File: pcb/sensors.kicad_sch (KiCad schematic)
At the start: 0 parts

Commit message: add sensors, hierarchical changes
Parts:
- added U?: MCP9804_DFN, Package_DFN_QFN:DFN-8-1EP_3x2mm_P0.5mm_EP1.7x1.4mm, symbol Sensor_Temperature:MCP9804_DFN
- added U?: INA230AIRGTT, Package_DFN_QFN:VQFN-16-1EP_3x3mm_P0.5mm_EP1.6x1.6mm, symbol Sensor_Current:INA230AIRGTT
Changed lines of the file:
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@@
 	(generator_version "9.0")
 	(paper "A4")
+	(symbol
+		(lib_id "Sensor_Temperature:MCP9804_DFN")
+		(at 130.81 54.61 0)
+		(unit 1)
+		(exclude_from_sim no)
+		(in_bom yes)
+		(on_board yes)
+		(dnp no)
+		(fields_autoplaced yes)
+		(property "Reference" "U?"
+			(at 146.05 48.1898 0)
+			(effects
+				(font
+					(size 1.27 1.27)
+				)
+			)
+		)
+		(property "Value" "MCP9804_DFN"
+			(at 146.05 50.7298 0)
+			(effects
+				(font
+					(size 1.27 1.27)
+				)
+			)
+		)
+		(property "Footprint" "Package_DFN_QFN:DFN-8-1EP_3x2mm_P0.5mm_EP1.7x1.4mm"
+			(at 130.81 54.61 0)
+			(effects
+				(font
+					(size 1.27 1.27)
+				)
+				(hide yes)
+			)
+		)
+		(property "Datasheet" "http://ww1.microchip.com/downloads/en/DeviceDoc/22203b.pdf"
+			(at 124.46 43.18 0)
+			(effects
+				(font
+					(size 1.27 1.27)
+				)
+				(hide yes)
+			)
+		)
+		(property "Description" "±0.25°C (±1°C) Typical (Maximum), Digital Temperature Sensor, DFN-8"
+			(at 130.81 54.61 0)
+			(effects
+				(font
+					(size 1.27 1.27)
+				)
+				(hide yes)
+			)
+		)
+		(pin "8"
+		)
+		(pin "3"
+		)
+		(pin "2"
+		)
+		(pin "1"
+		)
+		(pin "5"
+		)
+		(pin "7"
+		)
+		(pin "6"
+		)
+		(pin "4"
+		)
+		(pin "9"
+		)
+		(instances
+			(project ""
+				(path "/e63e39d7-6ac0-4ffd-8aa3-1841a4541b55/010325a2-ae86-4ae0-96e8-1d16e8e45471"
+					(reference "U?")
+					(unit 1)
+				)
+			)
+		)
+	)
+	(symbol
+		(lib_id "Sensor_Current:INA230AIRGTT")
+		(at 73.66 55.88 0)
+		(unit 1)
+		(exclude_from_sim no)
+		(in_bom yes)
+		(on_board yes)
+		(dnp no)
+		(fields_autoplaced yes)
+		(property "Reference" "U?"
+			(at 73.66 36.83 0)
+			(effects
+				(font
+					(size 1.27 1.27)
+				)
+			)
+		)
+		(property "Value" "INA230AIRGTT"
+			(at 73.66 39.37 0)
+			(effects
+				(font
+					(size 1.27 1.27)
+				)
+			)
+		)
+		(property "Footprint" "Package_DFN_QFN:VQFN-16-1EP_3x3mm_P0.5mm_EP1.6x1.6mm"
+			(at 73.66 55.88 0)
+			(effects
+				(font
+					(size 1.27 1.27)
+				)
+				(hide yes)
+			)
+		)
+		(property "Datasheet" "https://www.ti.com/lit/ds/symlink/ina230.pdf?ts=1755978668271"
+			(at 73.66 55.88 0)
+			(effects
+				(font
+					(size 1.27 1.27)
+				)
+				(hide yes)
+			)
+		)
+		(property "Description" "36-V, 16-bit, I²C output current, voltage and power monitor with alert"
+			(at 73.66 55.88 0)
+			(effects
+				(font
+					(size 1.27 1.27)
+				)
+				(hide yes)
+			)
+		)
+		(pin "15"
+		)
+		(pin "17"
+		)
+		(pin "10"
+		)
+		(pin "4"
+		)
+		(pin "5"
+		)
+		(pin "16"
+		)
+		(pin "1"
+		)
+		(pin "12"
+		)
+		(pin "3"
+		)
+		(pin "11"
+		)
+		(pin "13"
+		)
+		(pin "2"
+		)
+		(pin "6"
+		)
+		(pin "7"
+		)
+		(pin "8"
+		)
+		(pin "8"
+		)
+		(pin "14"
+		)
+		(instances
+			(project ""
+				(path "/e63e39d7-6ac0-4ffd-8aa3-1841a4541b55/010325a2-ae86-4ae0-96e8-1d16e8e45471"
+					(reference "U?")
+					(unit 1)
+				)
+			)
+		)
+	)
 )

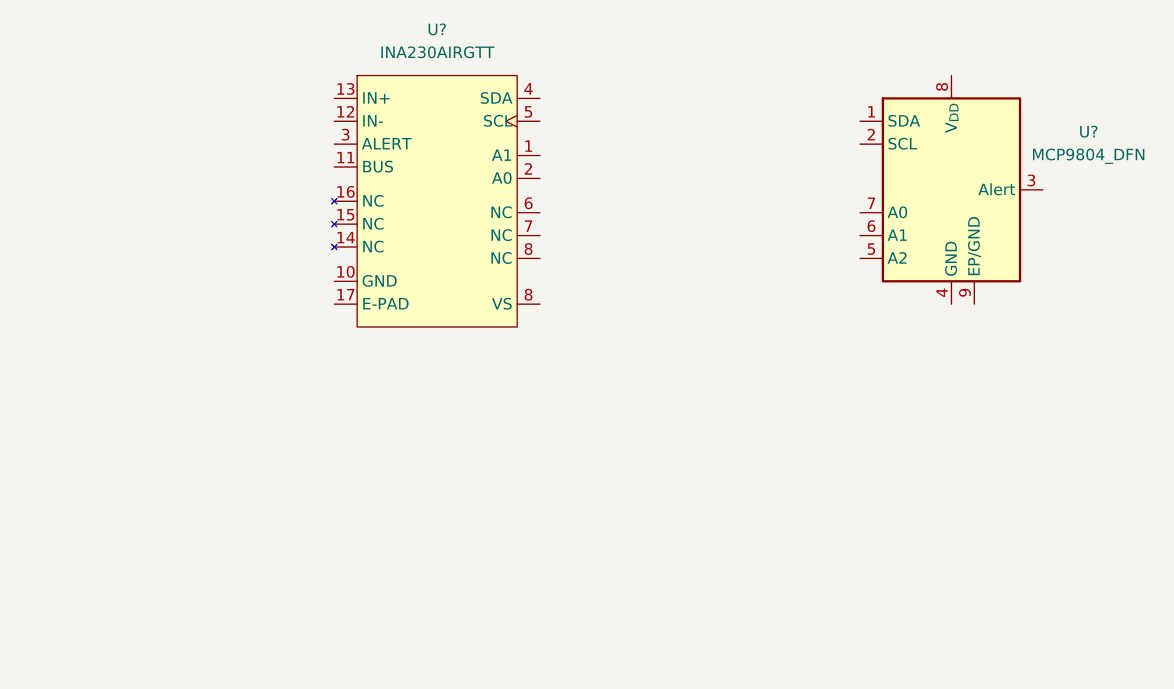
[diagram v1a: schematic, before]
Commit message: addl. updates to power hierarchy
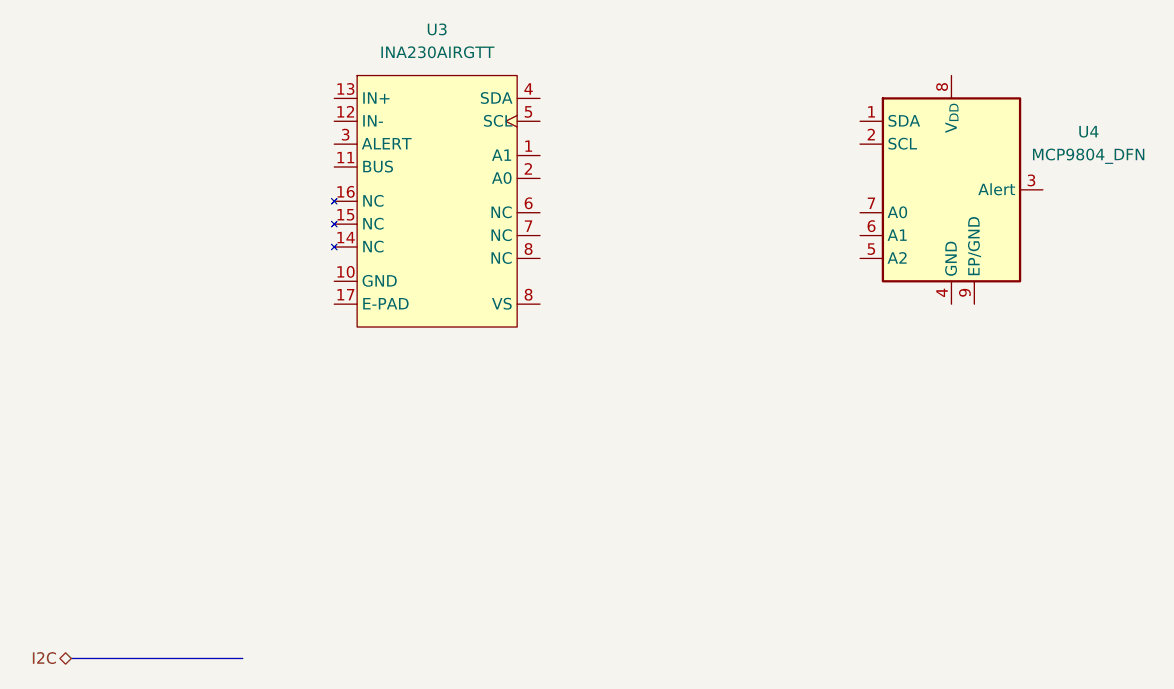
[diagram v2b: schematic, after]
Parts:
- gave numbers to parts that had none: 2
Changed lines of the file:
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@@
 	(generator_version "9.0")
 	(paper "A4")
+	(bus
+		(pts
+			(xy 33.02 106.68) (xy 52.07 106.68)
+		)
+		(stroke
+			(width 0)
+			(type default)
+		)
+	)
+	(hierarchical_label "I2C"
+		(shape bidirectional)
+		(at 33.02 106.68 180)
+		(effects
+			(font
+				(size 1.27 1.27)
+			)
+			(justify right)
+		)
+	)
 	(symbol
 		(lib_id "Sensor_Temperature:MCP9804_DFN")
@@
 		(dnp no)
 		(fields_autoplaced yes)
-		(property "Reference" "U?"
+		(property "Reference" "U4"
 			(at 146.05 48.1898 0)
 			(effects
@@
 			(project ""
 				(path "/e63e39d7-6ac0-4ffd-8aa3-1841a4541b55/010325a2-ae86-4ae0-96e8-1d16e8e45471"
-					(reference "U?")
+					(reference "U4")
 					(unit 1)
 				)
@@
 		(dnp no)
 		(fields_autoplaced yes)
-		(property "Reference" "U?"
+		(property "Reference" "U3"
 			(at 73.66 36.83 0)
 			(effects
@@
 			(project ""
 				(path "/e63e39d7-6ac0-4ffd-8aa3-1841a4541b55/010325a2-ae86-4ae0-96e8-1d16e8e45471"
-					(reference "U?")
+					(reference "U3")
 					(unit 1)
 				)

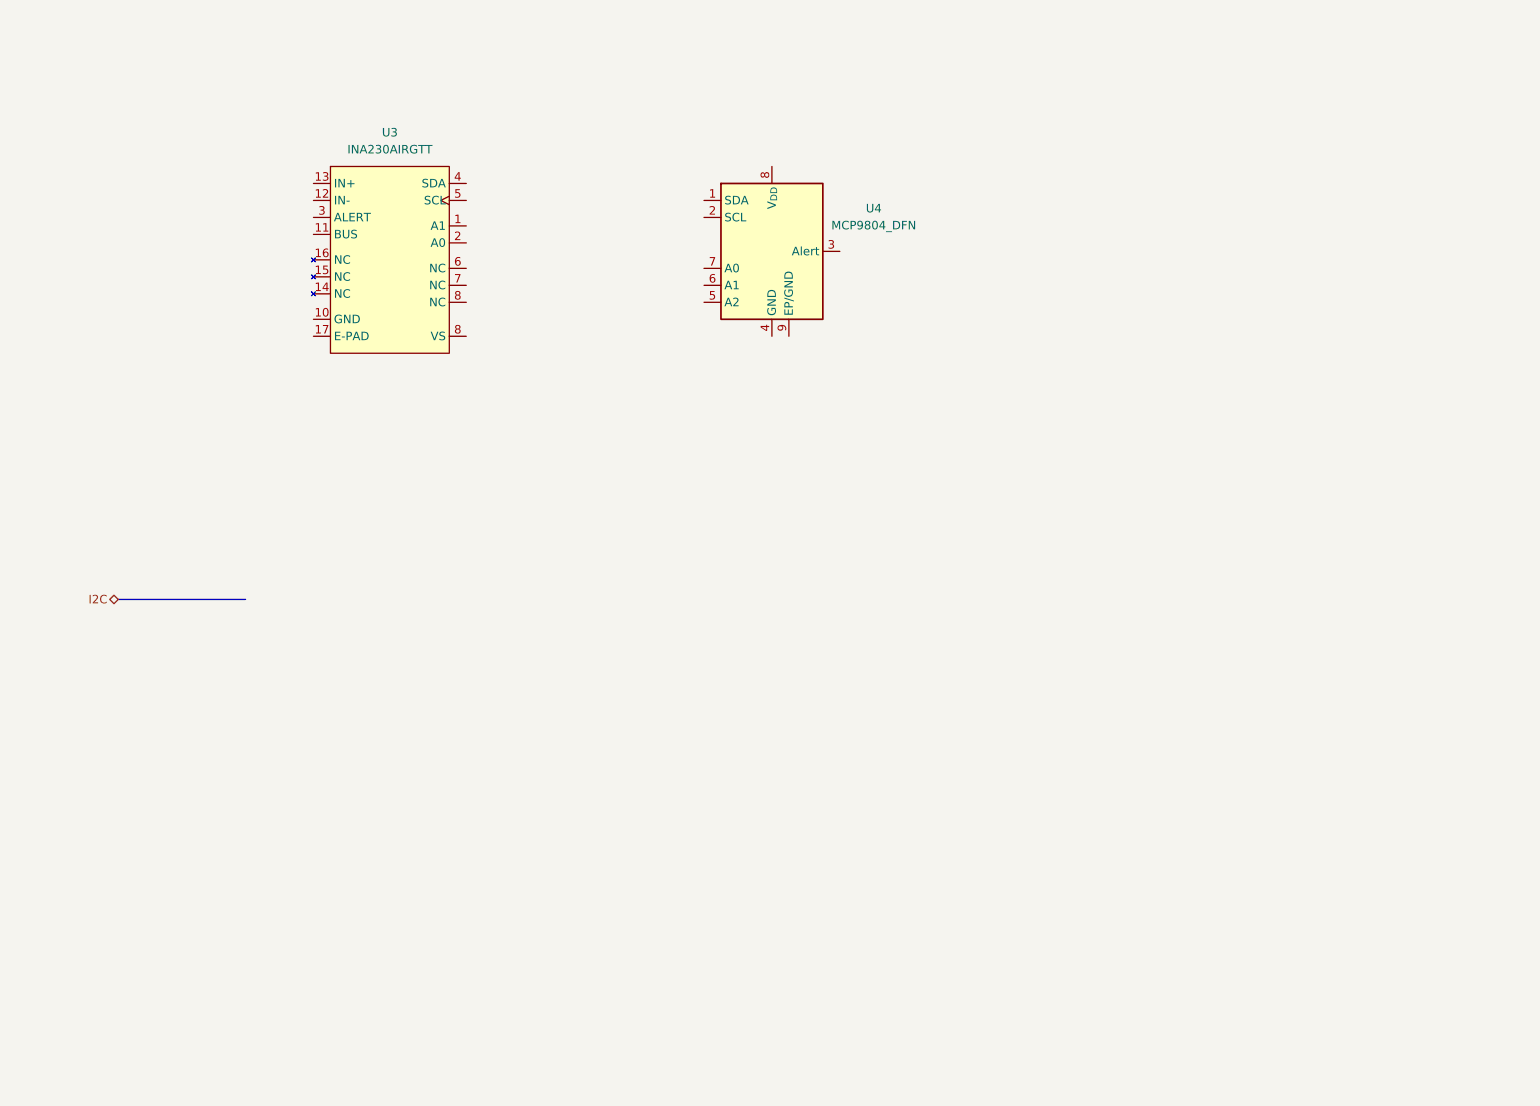
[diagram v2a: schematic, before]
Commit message: added power sequencing through raspi gpio
additionally defined sensors
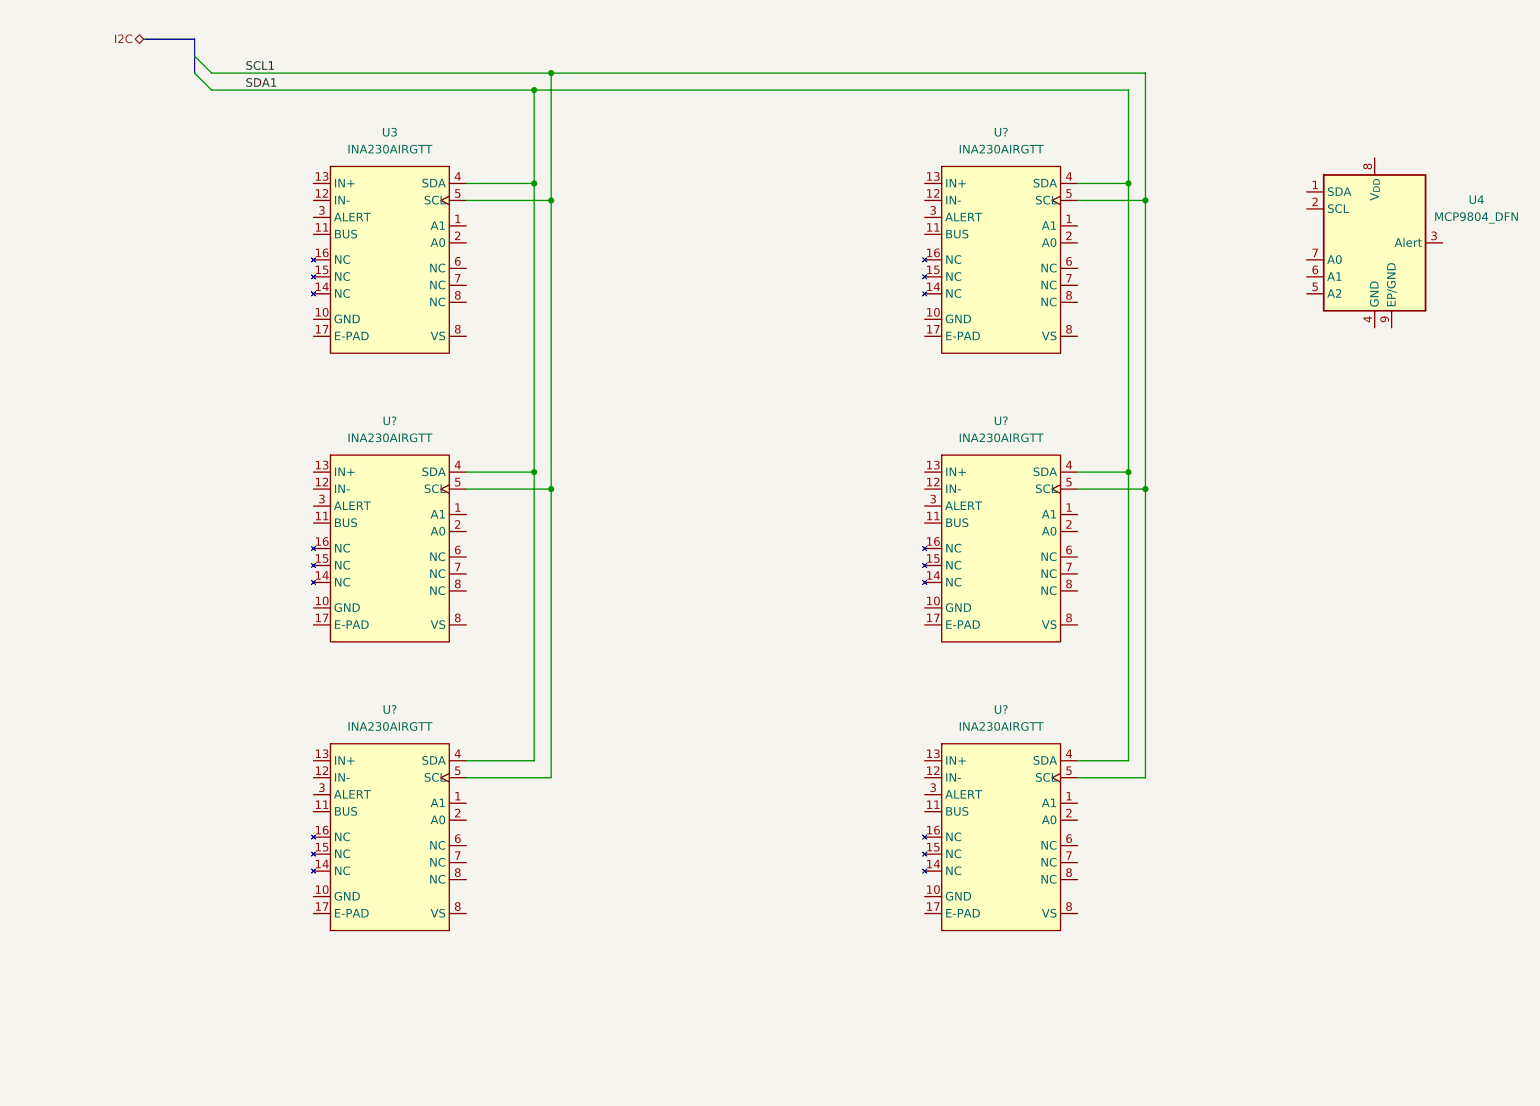
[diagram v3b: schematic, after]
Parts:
- added U? (x5): INA230AIRGTT, Package_DFN_QFN:VQFN-16-1EP_3x3mm_P0.5mm_EP1.6x1.6mm, symbol Sensor_Current:INA230AIRGTT
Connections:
- net SDA1: now reaches U3.4 (SDA)
- net SDA1: now also U?.4 (SDA), U?.4 (SDA), U?.4 (SDA), U?.4 (SDA), U?.4 (SDA)
- net SCL1: now reaches U3.5 (SCL)
- net SCL1: now also U?.5 (SCL), U?.5 (SCL), U?.5 (SCL), U?.5 (SCL), U?.5 (SCL)
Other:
- company: (none) -> Andre S Winkel
- title: (none) -> RPi HwAB HAT+
- moved on the sheet: U4

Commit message: quick edits to hierarchy
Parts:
- removed U? (x3): INA230AIRGTT, Package_DFN_QFN:VQFN-16-1EP_3x3mm_P0.5mm_EP1.6x1.6mm, symbol Sensor_Current:INA230AIRGTT
- added R3, R4: R_US, symbol Device:R_US
- gave numbers to parts that had none: 2
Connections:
- net SCL1: now also R4.2
- net SDA1: now also R3.2
- new net +3V3: R3.1, R4.1
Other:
- moved on the sheet: U3, U4, U6, U7

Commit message: added power supply simulations
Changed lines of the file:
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@@
 		(color 0 0 0 0)
 	)
+	(junction
+		(at 36.83 25.4)
+		(diameter 0)
+		(color 0 0 0 0)
+	)
+	(wire
+		(pts
+			(xy 26.67 25.4) (xy 36.83 25.4)
+		)
+		(stroke
+			(width 0)
+			(type default)
+		)
+	)
 	(wire
 		(pts
@@
 	(wire
 		(pts
-			(xy 20.32 25.4) (xy 50.8 25.4)
+			(xy 36.83 25.4) (xy 50.8 25.4)
 		)
 		(stroke
@@
 		(shape bidirectional)
 		(at 26.67 36.83 180)
+		(effects
+			(font
+				(size 1.27 1.27)
+			)
+			(justify right)
+		)
+	)
+	(hierarchical_label "+3V3"
+		(shape input)
+		(at 26.67 25.4 180)
 		(effects
 			(font
@@
 	(symbol
 		(lib_id "power:+3.3V")
-		(at 20.32 25.4 0)
+		(at 36.83 25.4 0)
 		(unit 1)
 		(exclude_from_sim no)
@@
 		(fields_autoplaced yes)
 		(property "Reference" "#PWR027"
-			(at 20.32 29.21 0)
+			(at 36.83 29.21 0)
 			(effects
 				(font
@@
 		)
 		(property "Value" "+3V3"
-			(at 20.32 20.32 0)
+			(at 36.83 20.32 0)
 			(effects
 				(font
@@
 		)
 		(property "Footprint" ""
-			(at 20.32 25.4 0)
+			(at 36.83 25.4 0)
 			(effects
 				(font
@@
 		)
 		(property "Datasheet" ""
-			(at 20.32 25.4 0)
+			(at 36.83 25.4 0)
 			(effects
 				(font
@@
 		)
 		(property "Description" "Power symbol creates a global label with name \"+3.3V\""
-			(at 20.32 25.4 0)
-			(effects
-				(font
+			(at 36.83 25.4 0)
+			(effects
+				(font
